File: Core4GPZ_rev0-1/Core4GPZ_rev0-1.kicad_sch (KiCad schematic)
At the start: 3 parts, among them U2 core4, U3 MPX4250

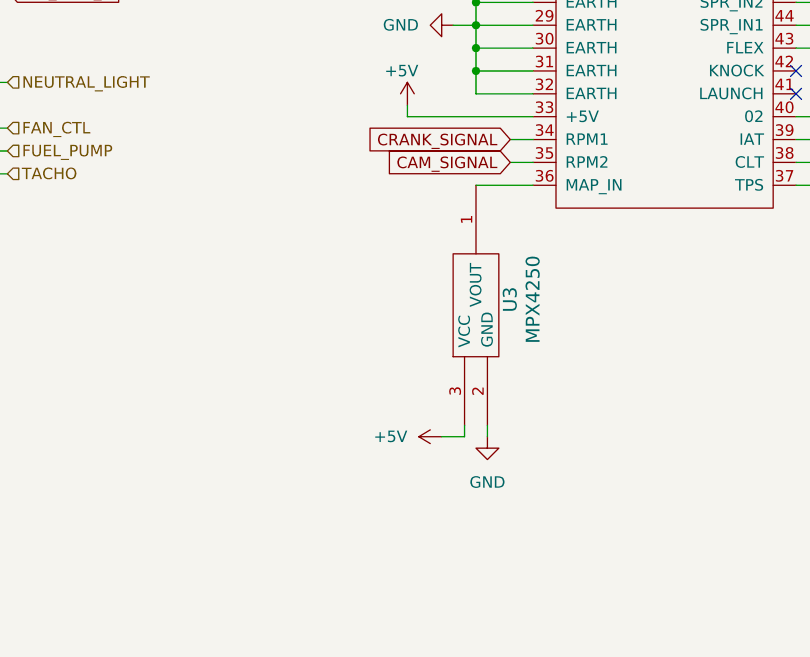
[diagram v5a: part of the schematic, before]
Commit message: Changed MAP sensors for MPXHZ6250AC6T1
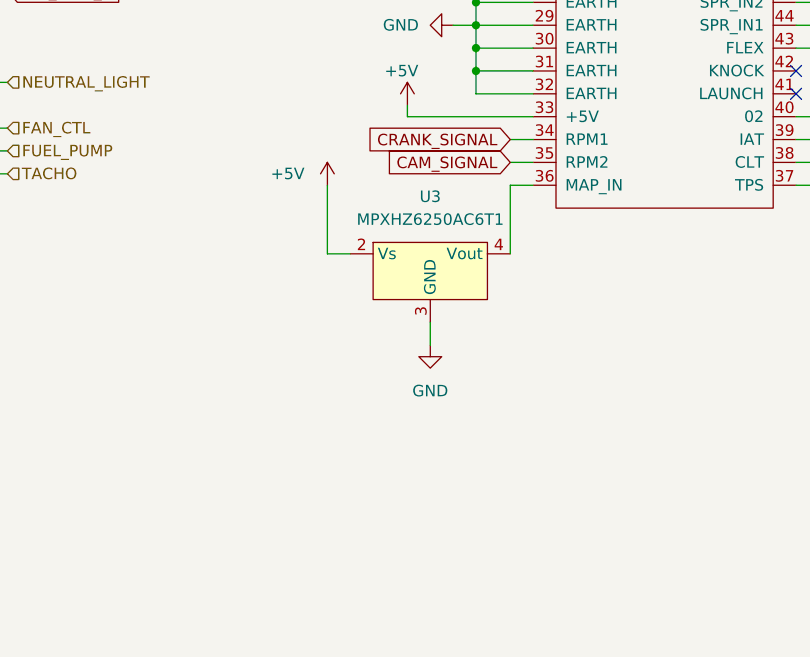
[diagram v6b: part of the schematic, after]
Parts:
- removed U3: MPX4250, Misc:MPX4250, symbol Speeduino_Misc:MPX4250
- added U3: MPXHZ6250AC6T1, IC_Automotive:MPXHZ6250AC6T1, symbol Speeduino_Misc:MPXHZ6250AC6T1
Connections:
- net +5V: now also U3.2 (Vs)
- net GND: now also U3.3 (GND)
- net at U2.36 (MAP_IN): now also U3.4 (Vout)
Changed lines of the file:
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@@
 	(wire
 		(pts
-			(xy 135.89 143.51) (xy 135.89 142.24)
-		)
-		(stroke
-			(width 0)
-			(type default)
-		)
-	)
-	(wire
-		(pts
 			(xy 50.8 91.44) (xy 53.34 91.44)
 		)
@@
 	(wire
 		(pts
-			(xy 138.43 142.24) (xy 138.43 143.51)
+			(xy 132.08 130.81) (xy 132.08 133.35)
 		)
 		(stroke
@@
 	(wire
 		(pts
-			(xy 137.16 115.57) (xy 143.51 115.57)
+			(xy 140.97 115.57) (xy 143.51 115.57)
 		)
 		(stroke
@@
 	(wire
 		(pts
+			(xy 120.65 115.57) (xy 120.65 123.19)
+		)
+		(stroke
+			(width 0)
+			(type default)
+		)
+	)
+	(wire
+		(pts
 			(xy 54.61 29.21) (xy 60.96 29.21)
 		)
@@
 	(wire
 		(pts
-			(xy 133.35 143.51) (xy 135.89 143.51)
-		)
-		(stroke
-			(width 0)
-			(type default)
-		)
-	)
-	(wire
-		(pts
 			(xy 172.72 110.49) (xy 175.26 110.49)
 		)
@@
 	(wire
 		(pts
+			(xy 140.97 123.19) (xy 140.97 115.57)
+		)
+		(stroke
+			(width 0)
+			(type default)
+		)
+	)
+	(wire
+		(pts
 			(xy 50.8 86.36) (xy 53.34 86.36)
 		)
@@
 		)
 	)
+	(wire
+		(pts
+			(xy 120.65 123.19) (xy 123.19 123.19)
+		)
+		(stroke
+			(width 0)
+			(type default)
+		)
+	)
 	(text "Inputs"
 		(exclude_from_sim no)
@@
 	(symbol
 		(lib_id "power:GND")
-		(at 138.43 143.51 0)
+		(at 132.08 133.35 0)
 		(unit 1)
 		(exclude_from_sim no)
@@
 		(fields_autoplaced yes)
 		(property "Reference" "#PWR05"
-			(at 138.43 149.86 0)
+			(at 132.08 139.7 0)
 			(effects
 				(font
@@
 		)
 		(property "Value" "GND"
-			(at 138.43 148.59 0)
+			(at 132.08 138.43 0)
 			(effects
 				(font
@@
 		)
 		(property "Footprint" ""
-			(at 138.43 143.51 0)
+			(at 132.08 133.35 0)
 			(effects
 				(font
@@
 		)
 		(property "Datasheet" ""
-			(at 138.43 143.51 0)
+			(at 132.08 133.35 0)
 			(effects
 				(font
@@
 		)
 		(property "Description" ""
-			(at 138.43 143.51 0)
+			(at 132.08 133.35 0)
 			(effects
 				(font
@@
 	)
 	(symbol
-		(lib_id "Speeduino_Misc:MPX4250")
-		(at 137.16 128.27 90)
-		(unit 1)
-		(exclude_from_sim no)
-		(in_bom yes)
-		(on_board yes)
-		(dnp no)
-		(property "Reference" "U3"
-			(at 140.97 128.27 0)
-			(effects
-				(font
-					(size 1.524 1.524)
-				)
-			)
-		)
-		(property "Value" "MPX4250"
-			(at 143.51 128.27 0)
-			(effects
-				(font
-					(size 1.524 1.524)
-				)
-			)
-		)
-		(property "Footprint" "Misc:MPX4250"
-			(at 125.73 128.27 0)
-			(effects
-				(font
-					(size 1.524 1.524)
-				)
-				(hide yes)
-			)
-		)
-		(property "Datasheet" ""
-			(at 137.16 129.54 0)
-			(effects
-				(font
-					(size 1.524 1.524)
-				)
-			)
-		)
-		(property "Description" ""
-			(at 137.16 128.27 0)
-			(effects
-				(font
-					(size 1.27 1.27)
-				)
-				(hide yes)
-			)
-		)
-		(pin "1"
-		)
-		(pin "2"
-		)
-		(pin "3"
-		)
-		(instances
-			(project "Core4GPZ_rev0-1"
-				(path "/ac28f42d-34b3-4fcc-84dd-ab6106f99610"
-					(reference "U3")
-					(unit 1)
-				)
-			)
-		)
-	)
-	(symbol
 		(lib_id "power:+12V")
 		(at 129.54 86.36 0)
@@
 	(symbol
 		(lib_id "power:+5V")
-		(at 133.35 143.51 90)
+		(at 120.65 115.57 0)
+		(mirror y)
 		(unit 1)
 		(exclude_from_sim no)
@@
 		(on_board yes)
 		(dnp no)
-		(fields_autoplaced yes)
 		(property "Reference" "#PWR03"
-			(at 137.16 143.51 0)
+			(at 120.65 119.38 0)
 			(effects
 				(font
@@
 		)
 		(property "Value" "+5V"
-			(at 129.54 143.51 90)
+			(at 118.11 114.2999 0)
 			(effects
 				(font
@@
 		)
 		(property "Footprint" ""
-			(at 133.35 143.51 0)
+			(at 120.65 115.57 0)
 			(effects
 				(font
@@
 		)
 		(property "Datasheet" ""
-			(at 133.35 143.51 0)
+			(at 120.65 115.57 0)
 			(effects
 				(font
@@
 		)
 		(property "Description" ""
-			(at 133.35 143.51 0)
+			(at 120.65 115.57 0)
 			(effects
 				(font
@@
 					(unit 1)
 				)
+			)
+		)
+	)
+	(symbol
+		(lib_id "Speeduino_Misc:MPXHZ6250AC6T1")
+		(at 132.08 125.73 0)
+		(unit 1)
+		(exclude_from_sim no)
+		(in_bom yes)
+		(on_board yes)
+		(dnp no)
+		(fields_autoplaced yes)
+		(property "Reference" "U3"
+			(at 132.08 116.84 0)
+			(effects
+				(font
+					(size 1.27 1.27)
+				)
+			)
+		)
+		(property "Value" "MPXHZ6250AC6T1"
+			(at 132.08 119.38 0)
+			(effects
+				(font
+					(size 1.27 1.27)
+				)
+			)
+		)
+		(property "Footprint" "IC_Automotive:MPXHZ6250AC6T1"
+			(at 132.588 137.16 0)
+			(effects
+				(font
+					(size 1.27 1.27)
+				)
+				(hide yes)
+			)
+		)
+		(property "Datasheet" ""
+			(at 130.81 128.27 0)
+			(effects
+				(font
+					(size 1.27 1.27)
+				)
+				(hide yes)
+			)
+		)
+		(property "Description" ""
+			(at 130.81 128.27 0)
+			(effects
+				(font
+					(size 1.27 1.27)
+				)
+				(hide yes)
+			)
+		)
+		(pin "3"
+		)
+		(pin "2"
+		)
+		(pin "4"
+		)
+		(instances
+			(project ""
+				(path "/ac28f42d-34b3-4fcc-84dd-ab6106f99610"
+					(reference "U3")
+					(unit 1)
+				)

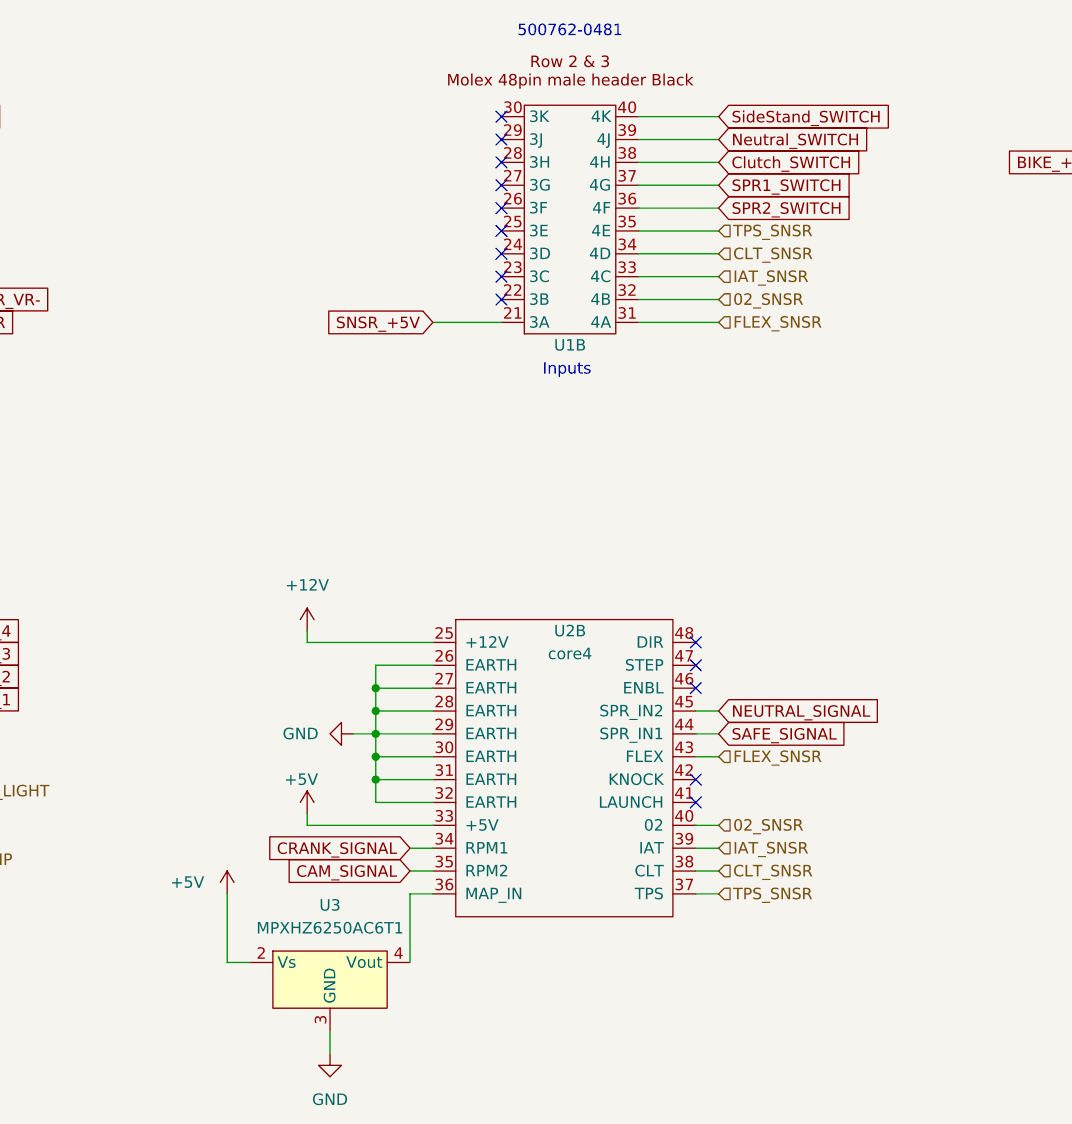
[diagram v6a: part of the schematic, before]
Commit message: Modified GND Plane. Reworked routing
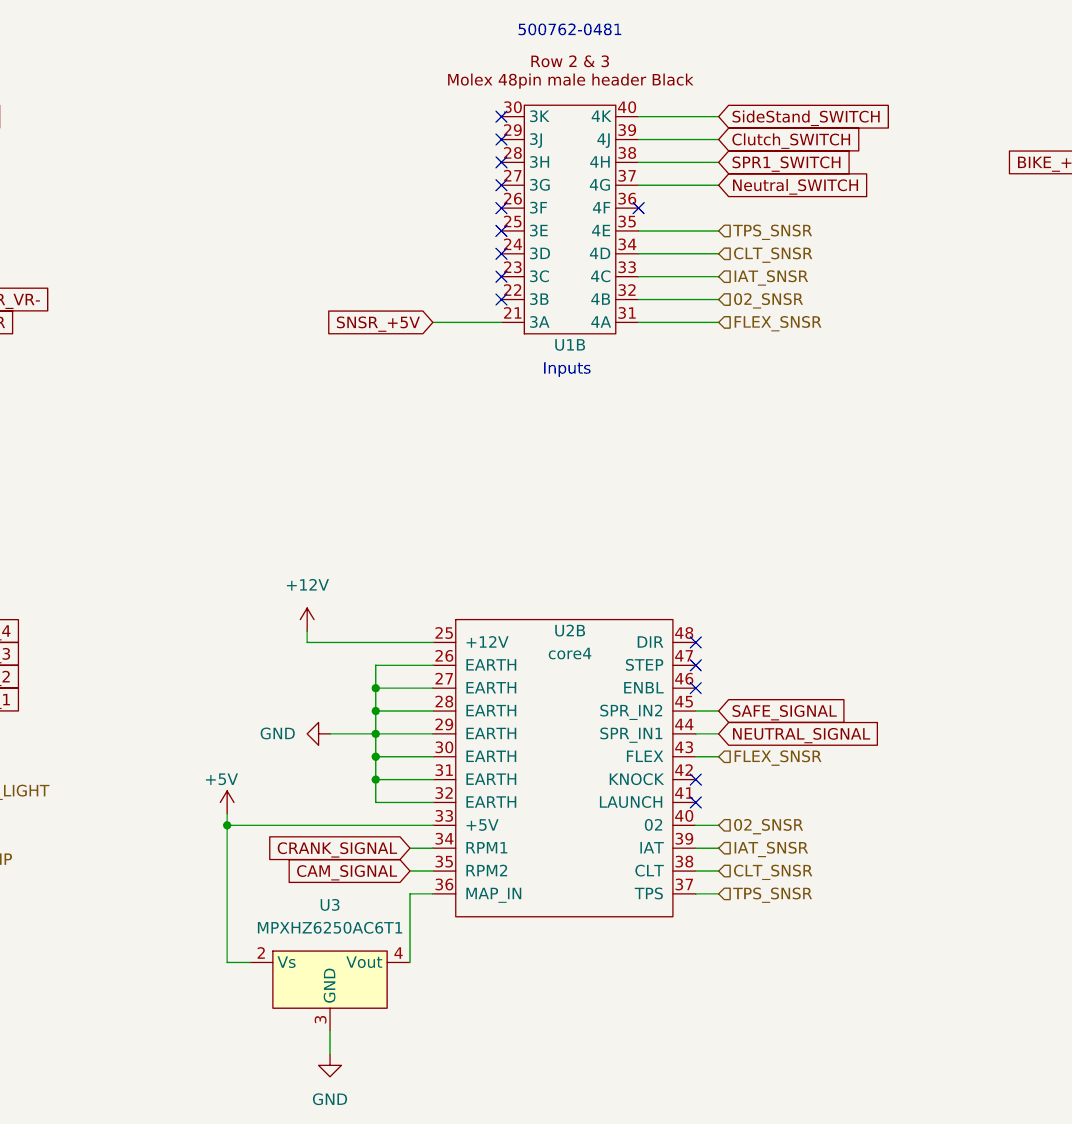
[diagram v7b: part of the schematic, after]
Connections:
- net Clutch_SWITCH: now also U1.39 (4J); no longer U1.38 (4H)
- net NEUTRAL_SIGNAL: now also U2.44 (SPR_IN1); no longer U2.45 (SPR_IN2)
- net Neutral_SWITCH: now also U1.37 (4G); no longer U1.39 (4J)
- net SAFE_SIGNAL: now also U2.45 (SPR_IN2); no longer U2.44 (SPR_IN1)
- net SPR1_SWITCH: now also U1.38 (4H); no longer U1.37 (4G)
- net SPR2_SWITCH: no longer names the net of U1.36 (4F)
- no-connect marks 45 -> 46
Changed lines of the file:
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@@
 	)
 	(junction
+		(at 120.65 107.95)
+		(diameter 0)
+		(color 0 0 0 0)
+	)
+	(junction
 		(at 137.16 100.33)
 		(diameter 0)
@@
 	)
 	(no_connect
+		(at 166.37 39.37)
+	)
+	(no_connect
 		(at 53.34 106.68)
 	)
@@
 	(wire
 		(pts
-			(xy 120.65 115.57) (xy 120.65 123.19)
-		)
-		(stroke
-			(width 0)
-			(type default)
-		)
-	)
-	(wire
-		(pts
 			(xy 54.61 29.21) (xy 60.96 29.21)
 		)
@@
 	(wire
 		(pts
-			(xy 129.54 107.95) (xy 143.51 107.95)
+			(xy 120.65 107.95) (xy 143.51 107.95)
 		)
 		(stroke
@@
 	(wire
 		(pts
-			(xy 166.37 39.37) (xy 175.26 39.37)
-		)
-		(stroke
-			(width 0)
-			(type default)
-		)
-	)
-	(wire
-		(pts
 			(xy 256.54 44.45) (xy 256.54 41.91)
 		)
@@
 	(wire
 		(pts
-			(xy 129.54 106.68) (xy 129.54 107.95)
+			(xy 120.65 106.68) (xy 120.65 107.95)
 		)
 		(stroke
@@
 	(wire
 		(pts
+			(xy 120.65 107.95) (xy 120.65 123.19)
+		)
+		(stroke
+			(width 0)
+			(type default)
+		)
+	)
+	(wire
+		(pts
 			(xy 137.16 95.25) (xy 137.16 97.79)
 		)
@@
 	(wire
 		(pts
-			(xy 137.16 97.79) (xy 134.62 97.79)
+			(xy 137.16 97.79) (xy 132.08 97.79)
 		)
 		(stroke
@@
 		)
 	)
-	(global_label "SPR2_SWITCH"
-		(shape input)
-		(at 175.26 39.37 0)
-		(fields_autoplaced yes)
-		(effects
-			(font
-				(size 1.27 1.27)
-			)
-			(justify left)
-		)
-		(property "Intersheetrefs" "${INTERSHEET_REFS}"
-			(at 191.0056 39.37 0)
-			(effects
-				(font
-					(size 1.27 1.27)
-				)
-				(justify left)
-				(hide yes)
-			)
-		)
-	)
 	(global_label "IGN_TRIG_1"
 		(shape input)
@@
 	(global_label "SAFE_SIGNAL"
 		(shape input)
-		(at 175.26 97.79 0)
+		(at 175.26 95.25 0)
 		(fields_autoplaced yes)
 		(effects
@@
 		)
 		(property "Intersheetrefs" "${INTERSHEET_REFS}"
-			(at 190.28 97.79 0)
+			(at 190.28 95.25 0)
 			(effects
 				(font
@@
 	(global_label "NEUTRAL_SIGNAL"
 		(shape input)
-		(at 175.26 95.25 0)
+		(at 175.26 97.79 0)
 		(fields_autoplaced yes)
 		(effects
@@
 		)
 		(property "Intersheetrefs" "${INTERSHEET_REFS}"
-			(at 193.9086 95.25 0)
+			(at 193.9086 97.79 0)
 			(effects
 				(font
@@
 	(global_label "Neutral_SWITCH"
 		(shape input)
-		(at 175.26 31.75 0)
+		(at 175.26 36.83 0)
 		(fields_autoplaced yes)
 		(effects
@@
 		)
 		(property "Intersheetrefs" "${INTERSHEET_REFS}"
-			(at 192.9408 31.75 0)
+			(at 192.9408 36.83 0)
 			(effects
 				(font
@@
 	(global_label "SPR1_SWITCH"
 		(shape input)
-		(at 175.26 36.83 0)
+		(at 175.26 34.29 0)
 		(fields_autoplaced yes)
 		(effects
@@
 		)
 		(property "Intersheetrefs" "${INTERSHEET_REFS}"
-			(at 191.0056 36.83 0)
+			(at 191.0056 34.29 0)
 			(effects
 				(font
@@
 	(global_label "Clutch_SWITCH"
 		(shape input)
-		(at 175.26 34.29 0)
+		(at 175.26 31.75 0)
 		(fields_autoplaced yes)
 		(effects
@@
 		)
 		(property "Intersheetrefs" "${INTERSHEET_REFS}"
-			(at 192.0941 34.29 0)
+			(at 192.0941 31.75 0)
 			(effects
 				(font
@@
 		(dnp no)
 		(fields_autoplaced yes)
-		(property "Reference" "#PWR05"
+		(property "Reference" "#PWR04"
 			(at 132.08 139.7 0)
 			(effects
@@
 			(project "Core4GPZ_rev0-1"
 				(path "/ac28f42d-34b3-4fcc-84dd-ab6106f99610"
-					(reference "#PWR05")
+					(reference "#PWR04")
 					(unit 1)
 				)
@@
 	(symbol
 		(lib_id "power:GND")
-		(at 134.62 97.79 270)
+		(at 132.08 97.79 270)
 		(unit 1)
 		(exclude_from_sim no)
@@
 		(dnp no)
 		(fields_autoplaced yes)
-		(property "Reference" "#PWR04"
-			(at 128.27 97.79 0)
+		(property "Reference" "#PWR03"
+			(at 125.73 97.79 0)
 			(effects
 				(font
@@
 		)
 		(property "Value" "GND"
-			(at 130.81 97.79 90)
+			(at 128.27 97.79 90)
 			(effects
 				(font
@@
 		)
 		(property "Footprint" ""
-			(at 134.62 97.79 0)
+			(at 132.08 97.79 0)
 			(effects
 				(font
@@
 		)
 		(property "Datasheet" ""
-			(at 134.62 97.79 0)
+			(at 132.08 97.79 0)
 			(effects
 				(font
@@
 		)
 		(property "Description" ""
-			(at 134.62 97.79 0)
+			(at 132.08 97.79 0)
 			(effects
 				(font
@@
 			(project "Core4GPZ_rev0-1"
 				(path "/ac28f42d-34b3-4fcc-84dd-ab6106f99610"
-					(reference "#PWR04")
+					(reference "#PWR03")
 					(unit 1)
 				)
@@
 	(symbol
 		(lib_id "power:+5V")
-		(at 129.54 106.68 0)
+		(at 120.65 106.68 0)
 		(unit 1)
 		(exclude_from_sim no)
@@
 		(on_board yes)
 		(dnp no)
-		(property "Reference" "#PWR02"
-			(at 129.54 110.49 0)
+		(property "Reference" "#PWR01"
+			(at 120.65 110.49 0)
 			(effects
 				(font
@@
 		)
 		(property "Value" "+5V"
-			(at 127 102.87 0)
+			(at 118.11 102.87 0)
 			(effects
 				(font
@@
 		)
 		(property "Footprint" ""
-			(at 129.54 106.68 0)
+			(at 120.65 106.68 0)
 			(effects
 				(font
@@
 		)
 		(property "Datasheet" ""
-			(at 129.54 106.68 0)
+			(at 120.65 106.68 0)
 			(effects
 				(font
@@
 		)
 		(property "Description" ""
-			(at 129.54 106.68 0)
+			(at 120.65 106.68 0)
 			(effects
 				(font
@@
 			(project "Core4GPZ_rev0-1"
 				(path "/ac28f42d-34b3-4fcc-84dd-ab6106f99610"
-					(reference "#PWR02")
+					(reference "#PWR01")
 					(unit 1)
 				)
@@
 		(dnp no)
 		(fields_autoplaced yes)
-		(property "Reference" "#PWR01"
+		(property "Reference" "#PWR02"
 			(at 129.54 90.17 0)
 			(effects
@@
 			(project "Core4GPZ_rev0-1"
 				(path "/ac28f42d-34b3-4fcc-84dd-ab6106f99610"
-					(reference "#PWR01")
-					(unit 1)
-				)
-			)
-		)
-	)
-	(symbol
-		(lib_id "power:+5V")
-		(at 120.65 115.57 0)
-		(mirror y)
-		(unit 1)
-		(exclude_from_sim no)
-		(in_bom yes)
-		(on_board yes)
-		(dnp no)
-		(property "Reference" "#PWR03"
-			(at 120.65 119.38 0)
-			(effects
-				(font
-					(size 1.27 1.27)
-				)
-				(hide yes)
-			)
-		)
-		(property "Value" "+5V"
-			(at 118.11 114.2999 0)
-			(effects
-				(font
-					(size 1.27 1.27)
-				)
-				(justify left)
-			)
-		)
-		(property "Footprint" ""
-			(at 120.65 115.57 0)
-			(effects
-				(font
-					(size 1.27 1.27)
-				)
-				(hide yes)
-			)
-		)
-		(property "Datasheet" ""
-			(at 120.65 115.57 0)
-			(effects
-				(font
-					(size 1.27 1.27)
-				)
-				(hide yes)
-			)
-		)
-		(property "Description" ""
-			(at 120.65 115.57 0)
-			(effects
-				(font
-					(size 1.27 1.27)
-				)
-				(hide yes)
-			)
-		)
-		(pin "1"
-		)
-		(instances
-			(project "Core4GPZ_rev0-1"
-				(path "/ac28f42d-34b3-4fcc-84dd-ab6106f99610"
-					(reference "#PWR03")
+					(reference "#PWR02")
 					(unit 1)
 				)
@@
 		(dnp no)
 		(fields_autoplaced yes)
-		(property "Reference" "#PWR06"
+		(property "Reference" "#PWR05"
 			(at 222.25 109.22 0)
 			(effects
@@
 			(project "Core4GPZ_rev0-1"
 				(path "/ac28f42d-34b3-4fcc-84dd-ab6106f99610"
-					(reference "#PWR06")
+					(reference "#PWR05")
 					(unit 1)
 				)
